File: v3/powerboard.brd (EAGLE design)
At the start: 100 x 80 mm, 1 part, among them U1 TPS61088VQFN20

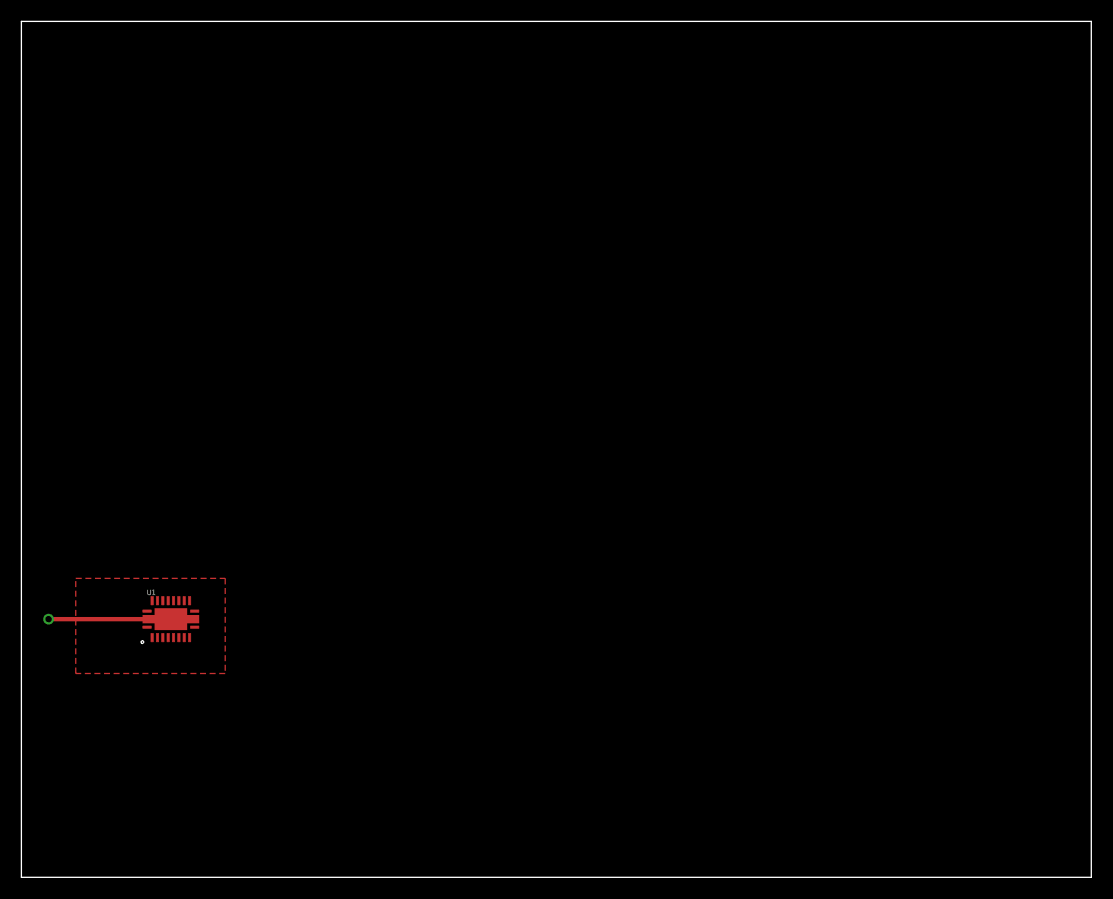
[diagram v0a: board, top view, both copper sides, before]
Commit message: 6v schematic complete.
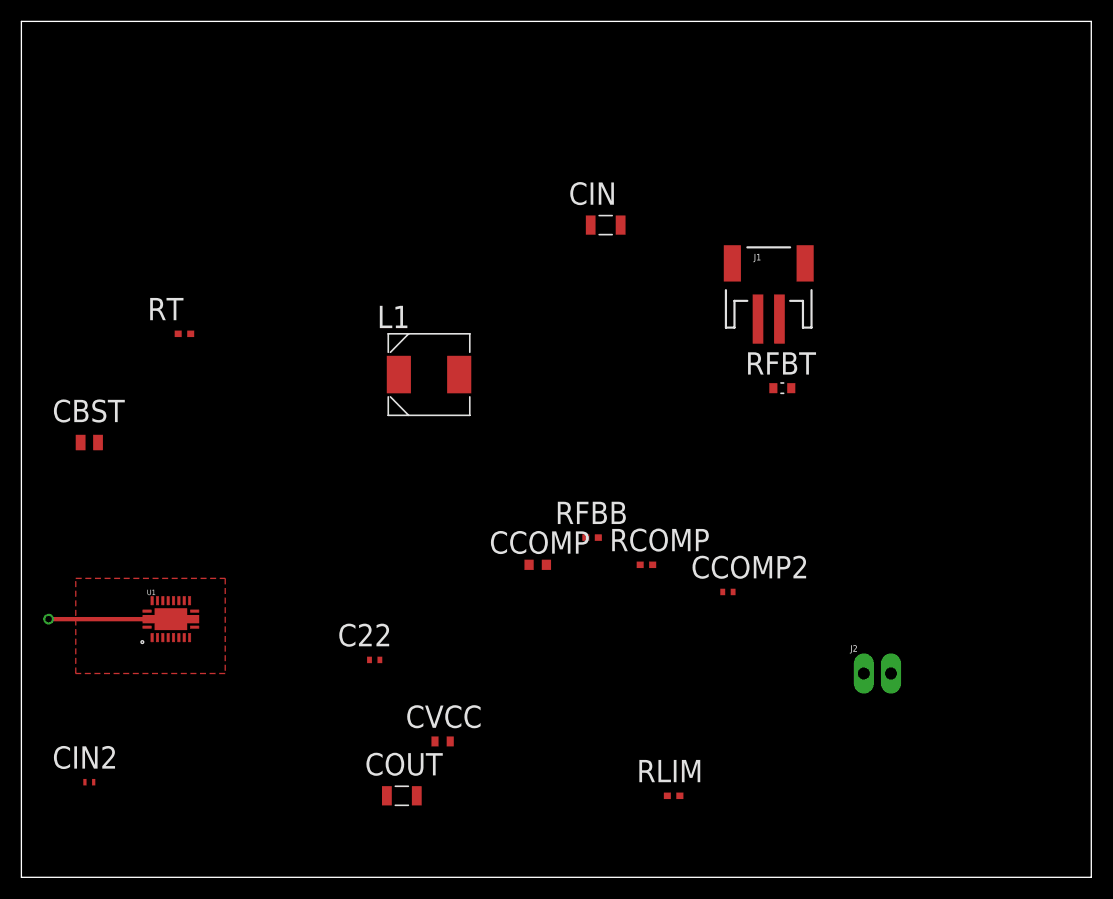
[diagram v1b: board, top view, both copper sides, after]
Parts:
- added C22: 8.2nF, Kemet_By_element14_Batch_1:CAPC1005X60N
- added CBST: 100nF, AVX_By_element14_Batch_1:CAPC2013X94N
- added CCOMP: 680PF, AVX_By_element14_Batch_1:CAPC1608X90N
- added CCOMP2: 36pF, Kemet_By_element14_Batch_1:CAPC1005X60N
- added CIN, COUT: 0.47uF, Kemet_By_element14_Batch_1:CAPC3216X180N
- added CIN2: 100nF, Murata_By_element14_Batch_1:CAPC1005X60N
- added CVCC: 1uF, Murata_By_element14_Batch_1:CAPC1608X85N
- added J1: (no value), SparkFun-Connectors:JST-2-SMD
- added J2: (no value), SparkFun-Connectors:1X02_LONGPADS
- added L1: DR73-1R0-R, Coiltronics_By_element14_Batch_1:INDM7676X355N
- added RCOMP: 38.3K Ohms, Vishay_By_element14_Batch_1:RESC1005X40N
- added RFBB: 118K Ohms, Vishay_By_element14_Batch_1:RESC1005X40N
- added RFBT: 470K Ohms, Yageo_By_element14_Batch_1:RESC1608X60N
- added RLIM: 102K Ohms, Vishay_By_element14_Batch_1:RESC1005X40N
- added RT: 261K Ohms, Vishay_By_element14_Batch_1:RESC1005X40N
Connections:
- new net BOOT: CBST.1, U1.P$8
- new net COMP: CCOMP2.2, RCOMP.1, U1.P$18
- new net ILIM: RLIM.1, U1.P$19
- new net N$1: CCOMP.2, RCOMP.2
- new net N$3: RT.1, U1.P$3
- new net N$4: RFBB.2, RFBT.2, U1.P$17
- new net SS: C22.2, U1.P$10
- new net SW: CBST.2, L1.1, RT.2, U1.P$4, U1.P$5, U1.P$6, U1.P$7
- new net VIN: CIN.2, CIN2.2, J1.2, L1.2, U1.P$9
- net GND: now also C22.1, CCOMP.1, CCOMP2.1, CIN.1, CIN2.1, COUT.1, CVCC.2, J1.1, J2.2, RFBB.1, RLIM.2, U1.P$11, U1.P$12
- net VCC: now also CVCC.1, U1.P$2
- net VOUT: now also COUT.2, J2.1, RFBT.1

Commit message: Progress on 6v eval board.
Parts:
- J1: device SparkFun-Connectors:JST-2-SMD -> SparkFun-Connectors:1X06_LONGPADS
- J2: device SparkFun-Connectors:1X02_LONGPADS -> SparkFun-Connectors:1X04_LONGPADS
- moved CIN 73.4 mm to (3.78, 8.05), turned to 90 degrees
- moved J1 64.3 mm to (14.7, 22.9), turned to 180 degrees
- moved J2 61.9 mm to (19.1, 2.54)
- moved RFBT 56.5 mm to (25.5, 12.4), turned to 90 degrees
- moved L1 44.0 mm to (7.62, 15.2), turned to 180 degrees
- moved CCOMP2 43.8 mm to (23.5, 16.2), turned to 270 degrees
- moved RLIM 39.7 mm to (22.2, 16.2), turned to 90 degrees
- moved RCOMP 37.4 mm to (24.1, 14.3)
- moved RT 36.5 mm to (14.9, 14.3), turned to 180 degrees
- moved RFBB 30.9 mm to (26.7, 16.2), turned to 270 degrees
- moved CBST 30.3 mm to (14.3, 11.4), turned to 90 degrees
- moved CCOMP 26.6 mm to (25.1, 16.2), turned to 270 degrees
- moved CVCC 23.0 mm to (16.8, 17.5), turned to 90 degrees
- moved C22 19.1 mm to (18.3, 8.07), turned to 90 degrees
- moved COUT 12.8 mm to (22.8, 7.59)
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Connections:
- net N$3 renamed FSW
- net N$4 renamed FB
- new net EN: J1.3, U1.P$2
- net GND: now also J1.2, J2.1, U1.P$22, U1.P$23, U1.P$24
- net VCC: no longer U1.P$2
- net VIN: now also J1.4, J1.5, J1.6; no longer J1.2
- net VOUT: now also J2.3, J2.4; no longer J2.1
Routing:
- net EN: track 0.00 -> 12.0 mm
- net GND: track 11.4 -> 0.00 mm, vias 1 -> 0
- net FB: track 0.00 -> 7.92 mm
- net COMP: track 0.00 -> 4.32 mm
- net BOOT: track 0.00 -> 3.50 mm
- net VCC: track 0.00 -> 2.48 mm
- net ILIM: track 0.00 -> 2.00 mm
- net FSW: track 0.00 -> 1.97 mm
- net SS: track 0.00 -> 1.92 mm
- net N$1: track 0.00 -> 1.23 mm
- added copper zone on layer 1, net SW
- added copper zone on layer 1, net VIN
- added copper zone on layer 1, net VOUT
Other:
- board size 100 x 80 mm -> 28.9 x 25.4 mm

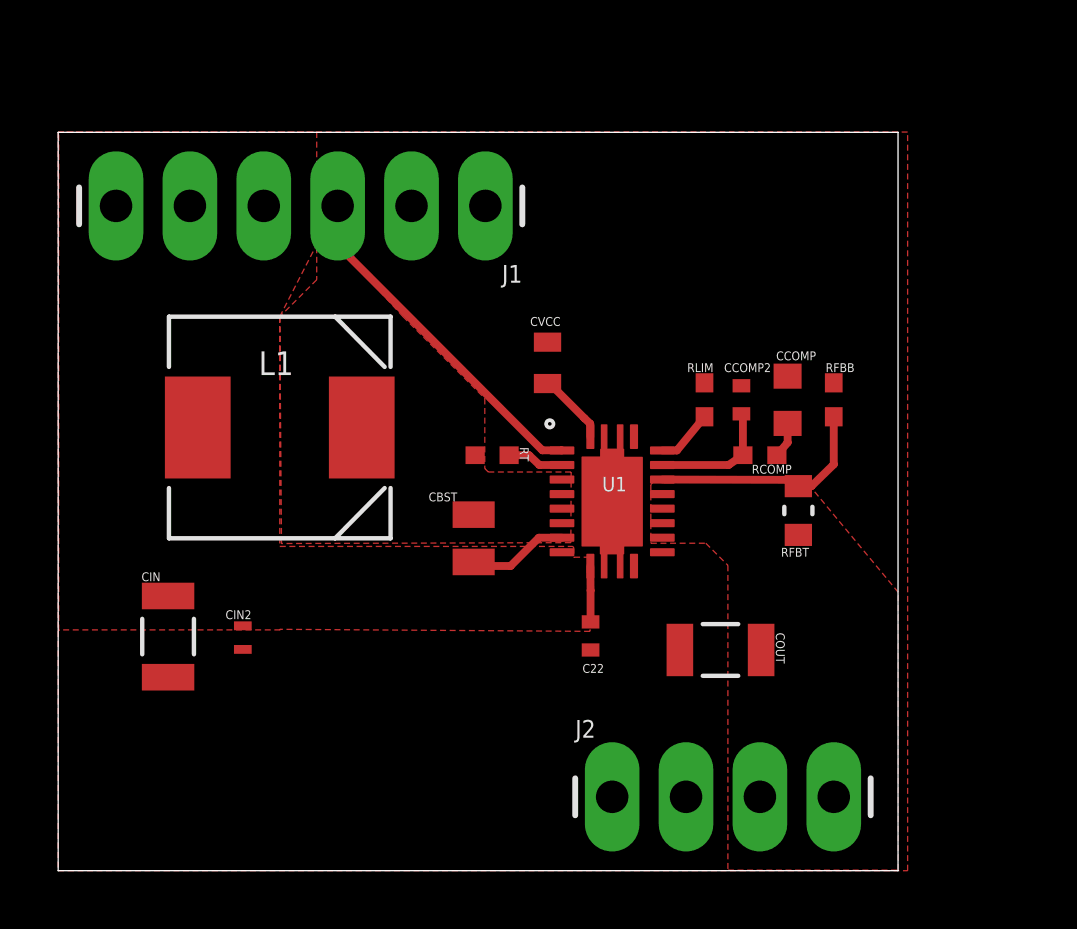
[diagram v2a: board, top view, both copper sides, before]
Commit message: Significant progress on layout for 6v eval.
TODO:
* bottom layer
* vias
* DRC errors in QFN part.
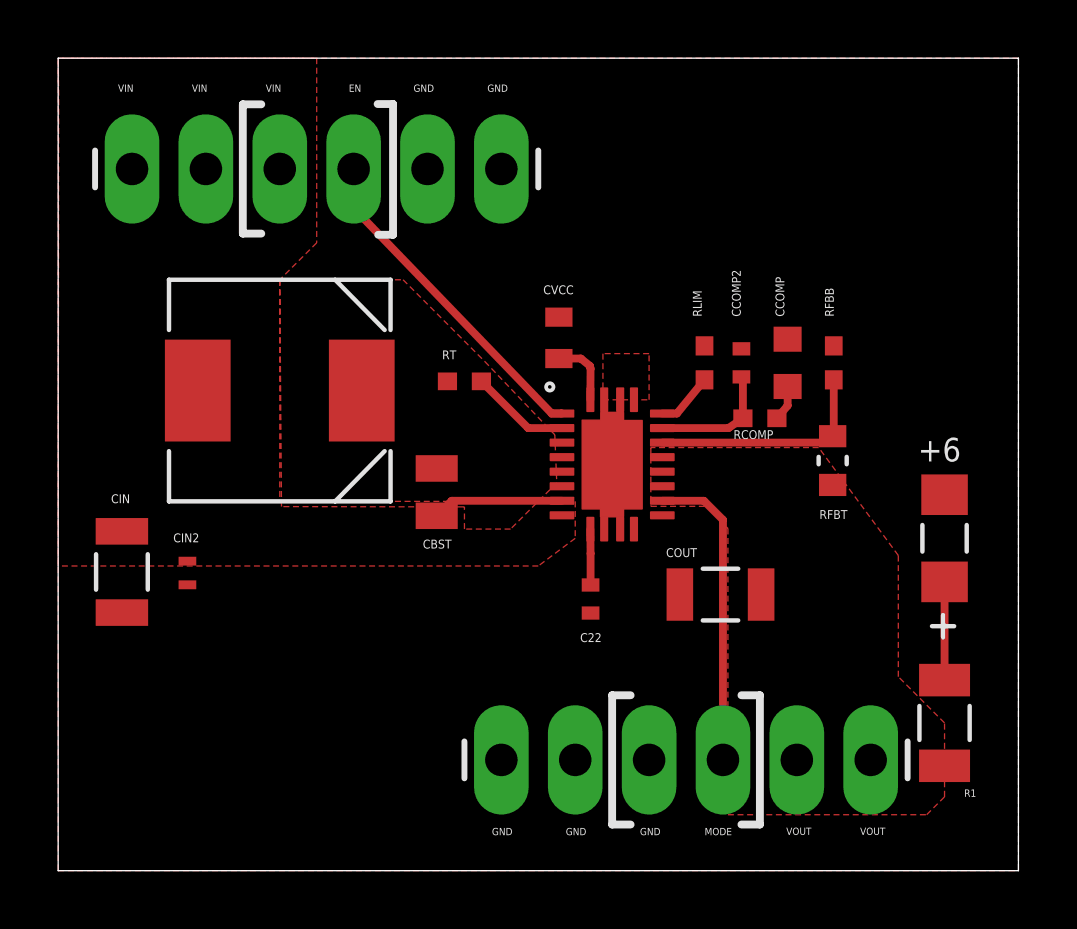
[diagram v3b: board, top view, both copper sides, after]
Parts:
- removed J2: (no value), SparkFun-Connectors:1X04_LONGPADS
- added +6: 597-3311-402F, Dialight_By_element14_Batch_1:LED_597-3311-402F
- added J4: (no value), SparkFun-Connectors:1X06_LONGPADS
- added R1: 200 Ohms, Vishay_By_element14_Batch_1:RESC3216X71N
- moved CIN2 2.93 mm to (4.45, 10.2)
- moved CIN 2.73 mm to (2.19, 10.3)
- moved RT 2.71 mm to (14.0, 16.8)
- moved RFBT 2.08 mm to (26.6, 14.1)
- moved CBST 2.03 mm to (13.0, 13.0)
- moved COUT 1.90 mm to (22.8, 9.49)
- moved J1 1.38 mm to (15.2, 24.1)
- moved L1 1.27 mm to (7.62, 16.5)
- moved U1 1.27 mm to (19.1, 14.0)
- moved C22 1.27 mm to (18.3, 9.34)
- moved CCOMP 1.27 mm to (25.1, 17.5)
- moved CCOMP2 1.27 mm to (23.5, 17.5)
- moved RCOMP 1.27 mm to (24.1, 15.6)
- moved RFBB 1.27 mm to (26.7, 17.5)
- moved RLIM 1.27 mm to (22.2, 17.5)
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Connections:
- new net LED_ANODE: +6.2, R1.1
- new net MODE: J4.4, U1.P$13
- net GND: now also +6.1, J4.1, J4.2, J4.3; no longer J2.1, J2.2
- net VOUT: now also J4.5, J4.6, R1.2; no longer J2.3, J2.4
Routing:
- net MODE: track 0.00 -> 10.6 mm
- net LED_ANODE: track 0.00 -> 3.38 mm
- net FSW: track 1.97 -> 3.46 mm
- net BOOT: track 3.50 -> 4.52 mm
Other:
- board size 28.9 x 25.4 mm -> 33 x 27.9 mm
- board text added: "EN"
- board text added: "GND"
- board text added: "MODE"
- board text added: "VIN"
- board text added: "VOUT"
